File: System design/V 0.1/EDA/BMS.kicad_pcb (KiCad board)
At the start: 2 copper layers, 26 x 70 mm, 20 parts, among them J1 Conn_01x03_Pin, J2 Conn_01x02_Pin, Q1 NMOS, Q2 NMOS, Q3 PMOS, Q4 PMOS, U1 SN74LVC2G14DBV, U2 SN74LVC2G14DBV, U3 CDSOT236-0504C

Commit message: Updated Directory
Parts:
- moved J2 16.6 mm to (151.5, 70.5)
- moved J1 7.61 mm to (139.7, 112.6)
- moved Q1 5.03 mm to (152.5, 87.9)
- moved Q2 5.03 mm to (152.5, 102.7)
- moved R5 3.49 mm to (144.2, 104.1)
- moved R6 3.45 mm to (138.7, 104.1)
- moved Q3 2.94 mm to (144.1, 97.0)
- moved Q4 2.94 mm to (139.5, 97.0)
- moved R7 2.58 mm to (144.5, 67.2)
- moved U3 2.02 mm to (145.2, 90.5)
- moved U2 2.02 mm to (138.9, 90.5)
- moved D1 2.00 mm to (139.0, 73.0)
- moved D2 2.00 mm to (144.5, 73.0)
- moved D3 2.00 mm to (139.0, 85.0)
- moved D4 2.00 mm to (144.5, 85.0)
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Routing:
- net Net-(D1-A): track 136.0 -> 103.1 mm
- net Net-(J2-Pin_1): track 43.5 -> 30.9 mm
- net Net-(D4-A): track 28.4 -> 17.7 mm
- net Net-(Q4-S): track 14.3 -> 9.97 mm
- net Net-(U3-IO2): track 29.4 -> 25.1 mm
- net Net-(Q3-S): track 35.3 -> 31.8 mm
- net Net-(J1-Pin_1): track 74.6 -> 72.3 mm
- net Net-(D2-K): track 22.0 -> 19.9 mm
- net Net-(Q1-S): track 12.2 -> 11.2 mm
- net Net-(Q4-G): track 13.3 -> 12.7 mm
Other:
- board size 26 x 70 mm -> 23.5 x 58.5 mm

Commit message: BMS Design Update
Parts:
- moved Q2 3.98 mm to (152.5, 98.8), turned to 90 degrees
- turned Q1 to -90 degrees
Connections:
- Q1 pad 2: unconnected-(Q1-G-Pad2) -> Net-(Q1-G)
- Q2 pad 2: unconnected-(Q2-G-Pad2) -> Net-(Q1-G)
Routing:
- net Net-(J1-Pin_1): track 72.3 -> 59.8 mm
- net Net-(J2-Pin_1): track 30.9 -> 21.7 mm, vias 0 -> 1
- net Net-(Q1-G): track 0.00 -> 8.32 mm
- net Net-(D4-A): track 17.7 -> 23.6 mm
- net Net-(D1-A): track 103.1 -> 107.4 mm
- net Net-(Q1-S): track 11.2 -> 9.44 mm
- net Net-(D1-K): track 23.2 -> 23.8 mm

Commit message: Updated with latest corrections
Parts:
- removed D1, D2, D3, D4: D_Capacitance, Capacitor_SMD:C_0805_2012Metric_Pad1.18x1.45mm_HandSolder
- added C1: C, Capacitor_SMD:C_0603_1608Metric_Pad1.08x0.95mm_HandSolder, F.Cu at (139.4, 73.0)
- added C2: C, Capacitor_SMD:C_0603_1608Metric_Pad1.08x0.95mm_HandSolder, F.Cu at (145.0, 73.0)
- added C3: C, Capacitor_SMD:C_0603_1608Metric_Pad1.08x0.95mm_HandSolder, F.Cu at (139.0, 85.0)
- added C4: C, Capacitor_SMD:C_0603_1608Metric_Pad1.08x0.95mm_HandSolder, F.Cu at (145.0, 85.0)
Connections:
- Q2 pad 3: unconnected-(Q2-S-Pad3) -> Net-(J2-Pin_1)
- U3 pad 1: unconnected-(U3-IO1-Pad1) -> Net-(J2-Pin_1)
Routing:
- net Net-(J2-Pin_1): track 21.7 -> 56.2 mm
- net Net-(J1-Pin_1): track 59.8 -> 76.3 mm
- net Net-(Q3-S): track 31.9 -> 39.1 mm, vias 0 -> 2
- net Net-(U3-VP): track 20.3 -> 26.9 mm
- net Net-(J1-Pin_2): track 107.4 -> 102.5 mm
- net Net-(U2-GND): track 23.6 -> 19.0 mm
- net Net-(U3-IO3): track 23.8 -> 22.5 mm

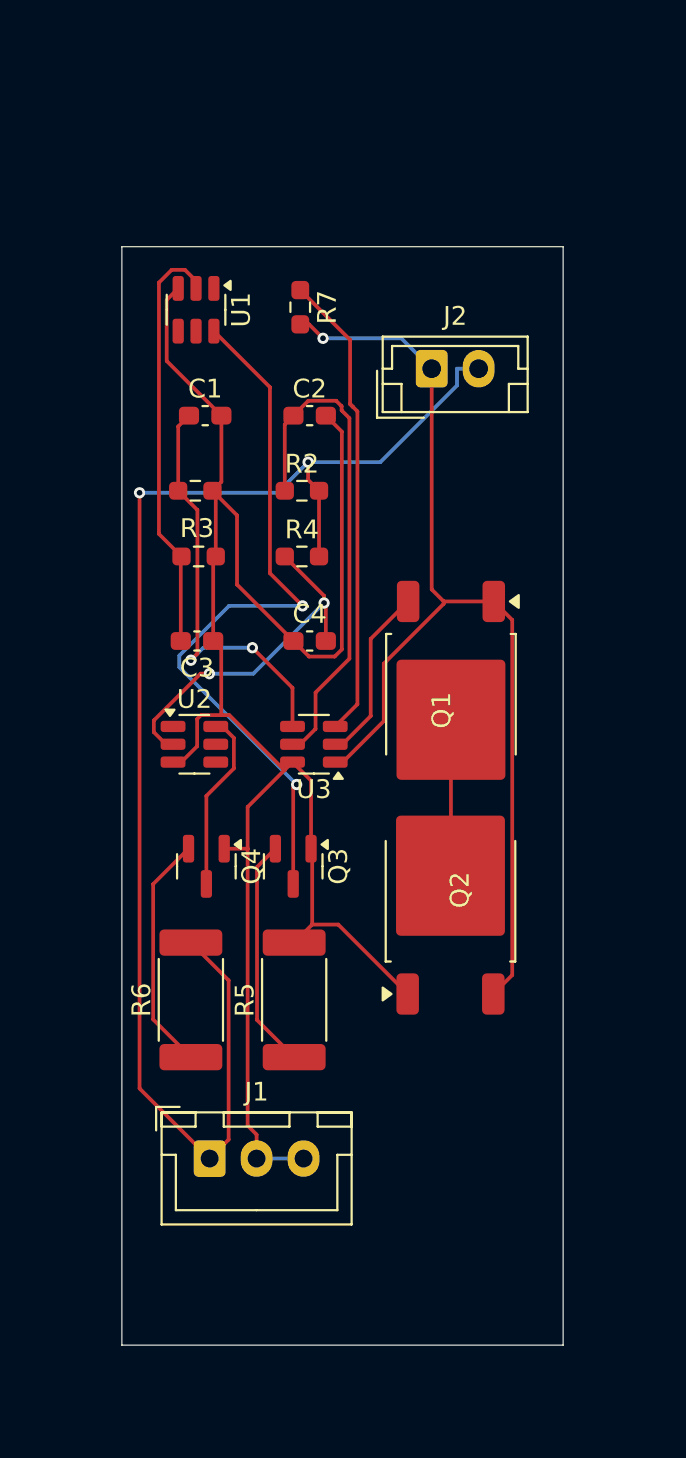
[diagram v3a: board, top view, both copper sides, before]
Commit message: Updated PCB (BMS)
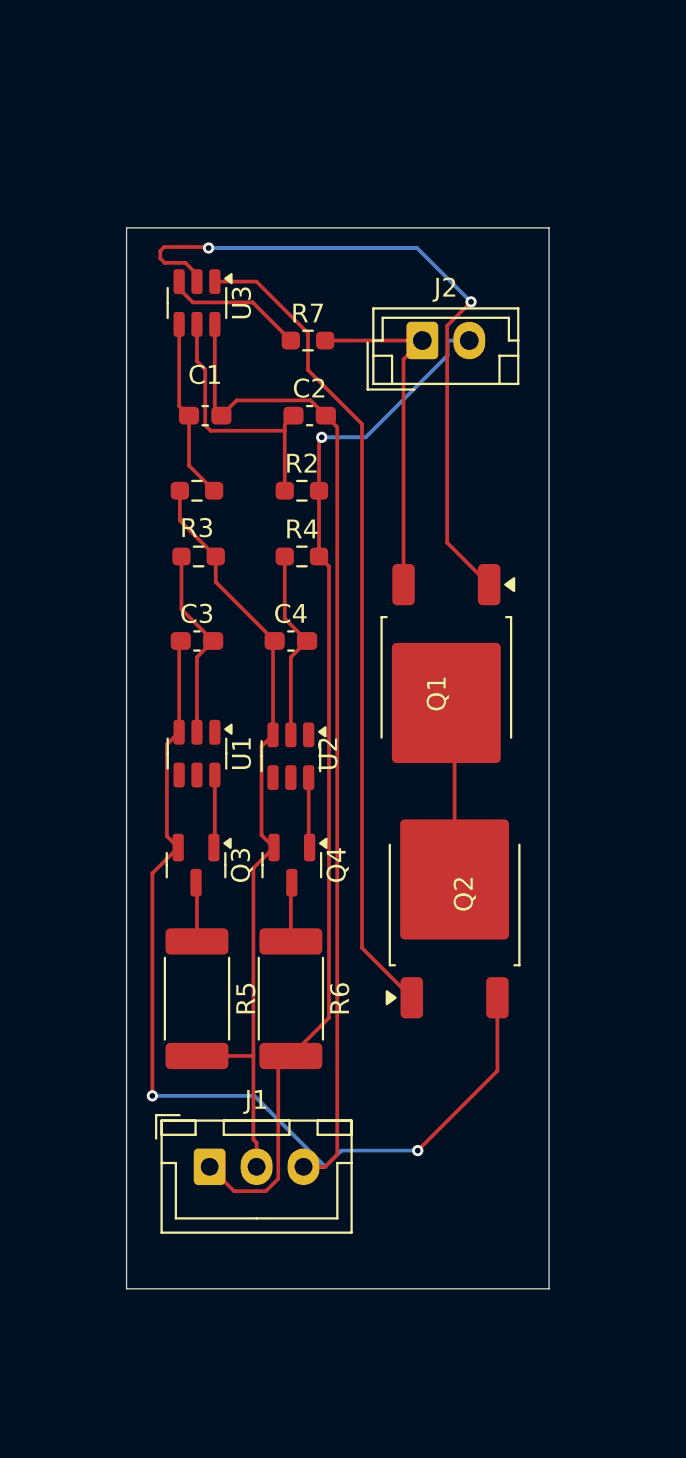
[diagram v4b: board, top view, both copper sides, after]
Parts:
- moved U3 24.3 mm to (139.0, 67.0), turned to -90 degrees
- moved U1 23.6 mm to (139.0, 91.0)
- moved R6 5.33 mm to (144.0, 104.0), turned to -90 degrees
- moved U2 5.18 mm to (144.0, 91.1), turned to -90 degrees
- moved Q3 5.18 mm to (138.9, 96.9)
- moved R5 5.18 mm to (139.0, 104.0), turned to -90 degrees
- moved Q4 4.55 mm to (144.1, 96.9)
- moved R7 1.82 mm to (144.9, 69.0), turned to 0 degrees
- moved J2 1.58 mm to (151.0, 69.0)
- moved C4 1.00 mm to (144.0, 85.0)
- moved Q1 0.93 mm to (152.3, 87.0)
- moved J1 0.44 mm to (139.7, 113.0)
- moved Q2 0.30 mm to (152.7, 99.0)
- moved R1 0.09 mm to (139.0, 77.0), turned to 0 degrees
- turned C3 to 0 degrees
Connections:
- C1 pad 2: Net-(J1-Pin_2) -> Net-(J1-Pin_3)
- C2 pad 2: Net-(J1-Pin_2) -> Net-(J1-Pin_3)
- C3 pad 1: Net-(J1-Pin_2) -> Net-(J1-Pin_3)
- J1 pad 3: Net-(J1-Pin_2) -> Net-(J1-Pin_3)
- Q1 pad 1: Net-(J2-Pin_1) -> Net-(Q1-D)
- Q1 pad 3: Net-(Q1-S) -> Net-(J2-Pin_1)
- Q2 pad 1: Net-(J1-Pin_2) -> Net-(Q2-D)
- Q2 pad 3: Net-(J2-Pin_1) -> Net-(J1-Pin_3)
- Q3 pad 1: Net-(J1-Pin_2) -> Net-(Q3-D)
- Q3 pad 2: Net-(Q3-G) -> Net-(J1-Pin_3)
- Q4 pad 1: Net-(J1-Pin_2) -> Net-(Q4-D)
- Q4 pad 2: Net-(Q4-G) -> Net-(J1-Pin_2)
- R5 pad 1: Net-(Q3-G) -> Net-(Q3-S)
- R6 pad 1: Net-(Q4-G) -> Net-(Q4-S)
- U1 pad 3: Net-(J1-Pin_2) -> Net-(J1-Pin_3)
- U1 pad 6: Net-(Q3-S) -> Net-(Q3-D)
- U2 pad 6: Net-(Q4-S) -> Net-(Q4-D)
- U3 pad 1: Net-(J2-Pin_1) -> Net-(Q2-D)
- U3 pad 2: Net-(Q1-S) -> Net-(Q1-D)
- U3 pad 6: Net-(J1-Pin_2) -> Net-(J1-Pin_3)
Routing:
- net Net-(J1-Pin_3): track 0.00 -> 105.4 mm, vias 0 -> 2
- net Net-(J1-Pin_2): track 102.5 -> 42.2 mm
- net Net-(Q2-D): track 0.00 -> 43.8 mm
- net Net-(J2-Pin_1): track 56.2 -> 18.6 mm, vias 1 -> 0
- net Net-(Q1-D): track 0.00 -> 37.4 mm, vias 0 -> 2
- net Net-(Q3-S): track 39.1 -> 3.15 mm, vias 2 -> 0
- net Net-(J1-Pin_1): track 76.3 -> 55.8 mm, vias 2 -> 1
- net Net-(U3-IO2): track 25.2 -> 7.47 mm
- net Net-(U3-IO3): track 22.5 -> 9.63 mm, vias 2 -> 0
- net Net-(U3-VP): track 26.9 -> 14.1 mm
- net Net-(Q4-G): track 12.7 -> 0.00 mm
- net Net-(Q3-G): track 12.3 -> 0.00 mm
- net Net-(U1-GND): track 22.5 -> 10.4 mm
- net Net-(Q1-S): track 9.44 -> 0.00 mm
- net Net-(U2-GND): track 19.0 -> 10.3 mm, vias 2 -> 0
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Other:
- board size 23.5 x 58.5 mm -> 22.5 x 56.5 mm

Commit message: PCB modified
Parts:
- added ARTS Lab: LOGO, LOGO, B.Cu at (144.5, 73.1)
- added USC: UofSC, LOGO, B.Cu at (144.5, 86.1)
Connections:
- net Net-(J2-Pin_1) renamed GND
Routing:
- net GND: track 18.6 -> 0.00 mm
- net Net-(Q1-D): track 37.4 -> 27.4 mm
- net Net-(J1-Pin_3): track 105.4 -> 100.9 mm, vias 2 -> 0
- net Net-(U3-VP): track 14.1 -> 15.4 mm
- net Net-(U3-IO2): track 7.47 -> 8.51 mm
- net Net-(Q2-D): track 43.8 -> 42.8 mm
- net Net-(J1-Pin_1): track 55.8 -> 55.1 mm
- added copper zone on B.Cu, net GND
- added copper zone on F.Cu, net GND
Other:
- board size 22.5 x 56.5 mm -> 27.5 x 61.5 mm
- board text added: "B+"
- board text added: "B-"
- board text added: "Bm"
- board text added: "P+"
- board text added: "P-"
